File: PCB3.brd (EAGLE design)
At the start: 94.7 x 52.2 mm, 138 parts, among them U1 PIC32MX570F512L, Y1 16MHz

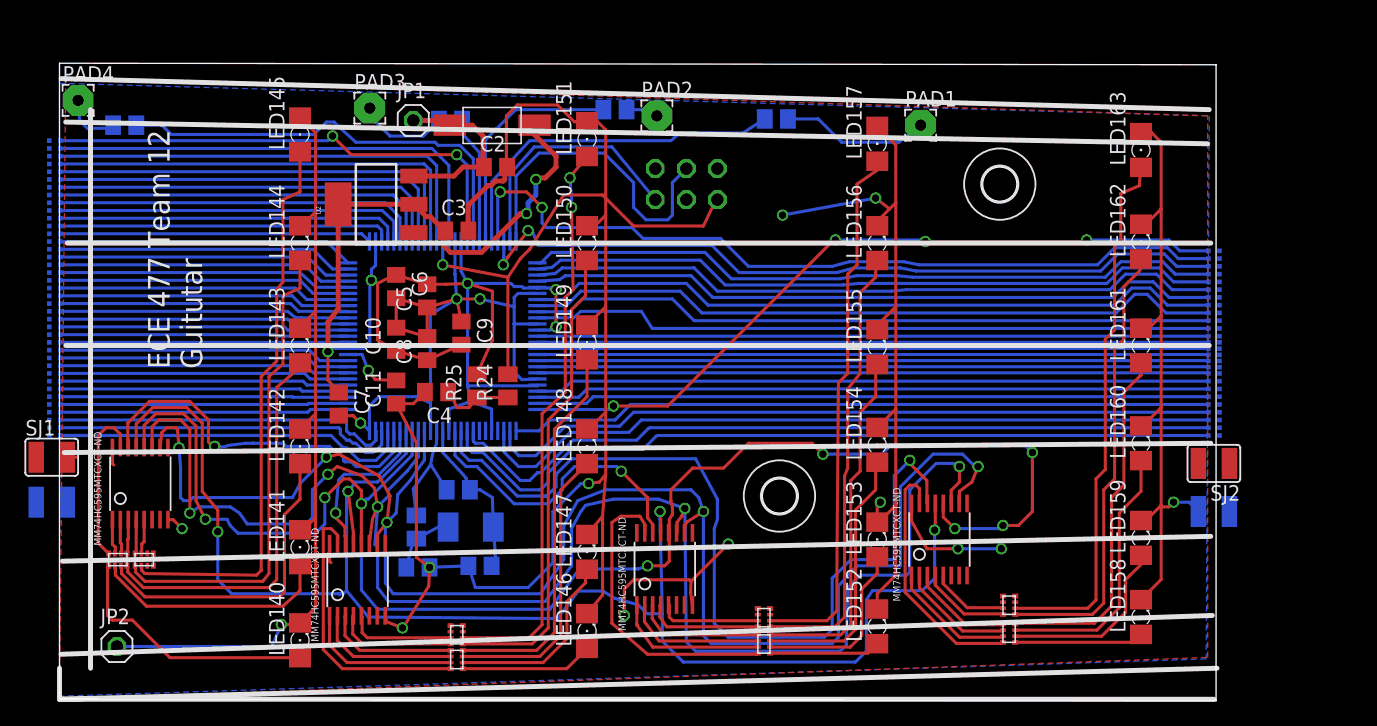
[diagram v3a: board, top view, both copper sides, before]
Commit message: Finished PCB3 checks and added traces for shift registers
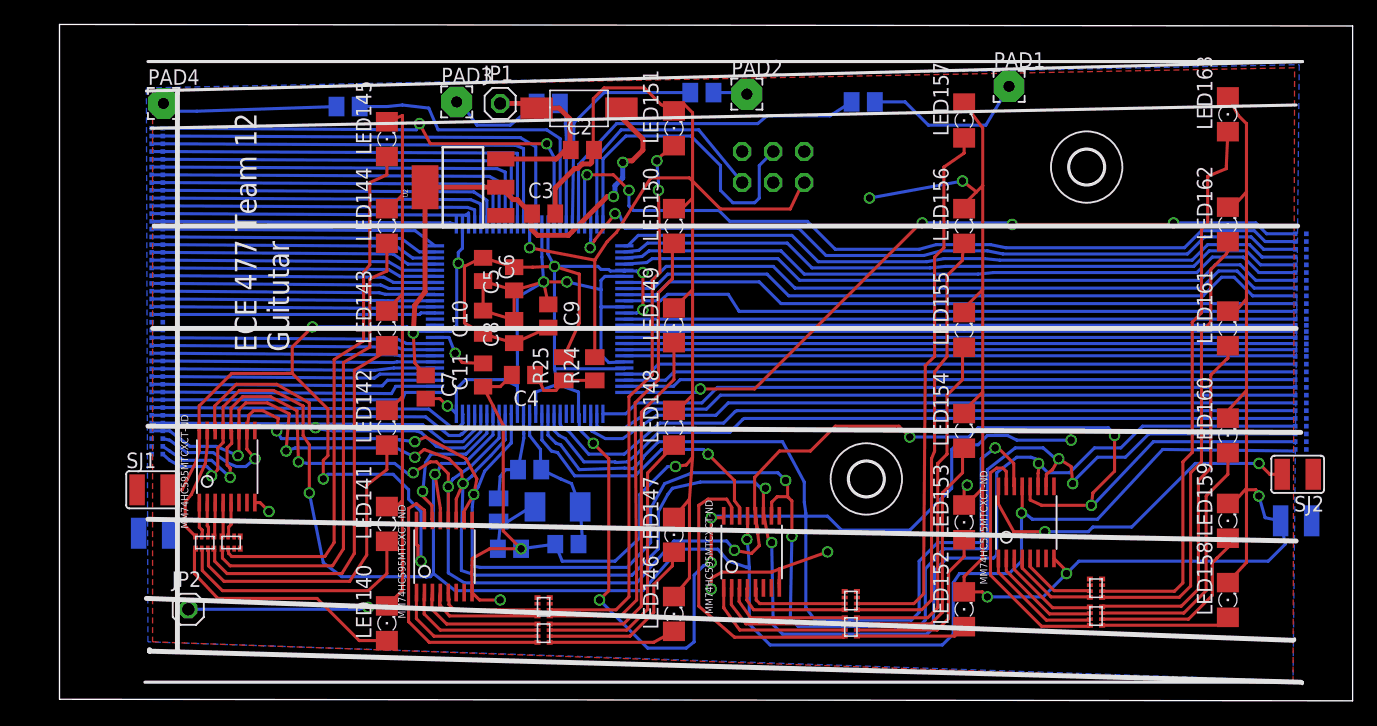
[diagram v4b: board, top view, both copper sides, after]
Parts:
- added RXD, U$2, U$79, U$80, U$81, U$82, U$83, U$84: JUMPER, ECE477_Guitutar:JUMPER
- moved R10 18.4 mm to (23.6, 48.5)
- moved SJ3 8.76 mm to (7.75, 13.6)
- moved SJ1 8.68 mm to (7.62, 17.1)
- moved U$43 8.44 mm to (8.00, 46.7)
- moved U$1 8.39 mm to (8.00, 44.8)
- moved U$10 8.39 mm to (8.00, 39.8)
- moved U$11 8.39 mm to (8.00, 39.1)
- moved U$12 8.39 mm to (8.00, 38.5)
- moved U$13 8.39 mm to (8.00, 37.8)
- moved U$14 8.39 mm to (8.00, 36.6)
- moved U$15 8.39 mm to (8.00, 37.2)
- moved U$16 8.39 mm to (8.00, 35.9)
- moved U$17 8.39 mm to (8.00, 35.3)
- moved U$18 8.39 mm to (8.00, 34.0)
- moved U$19 8.39 mm to (8.00, 34.7)
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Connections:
- net AMP: now also U$70.P$2
- net EAN: now also U$35.P$2
- net FRET1: now also U$18.P$2
- net FRET10: now also U$69.P$2
- net FRET11: now also U$48.P$2
- net FRET12: now also U$47.P$2
- net FRET13: now also U$52.P$2
- net FRET14: now also U$51.P$2
- net FRET15: now also U$56.P$2
- net FRET16: now also U$50.P$2
- net FRET17: now also U$55.P$2
- net FRET18: now also U$60.P$2
- net FRET19: now also U$59.P$2
- net FRET2: now also U$20.P$2
- net FRET20: now also U$58.P$2
- net FRET21: now also U$54.P$2
- net FRET22: now also U$64.P$2
- net FRET3: now also U$21.P$2
- net FRET4: now also U$22.P$2
- net FRET5: now also U$43.P$1, U$43.P$2
- net G: now also U$80.P$2, U$84.P$2
- net LED_SER1: now also U$12.P$2
- net LED_SER12: now also U$46.P$2
- net LED_SER13: now also U$53.P$2
- net LED_SER14: now also U$57.P$2
- net LED_SER15: now also U$49.P$2
- net LED_SER16: now also U$45.P$2
- net LED_SER17: now also U$63.P$2
- net LED_SER18: now also U$62.P$2
- net LED_SER19: now also U$61.P$2
- net LED_SER2: now also U$13.P$2
- net LED_SER20: now also U$68.P$2
- net LED_SER21: now also U$67.P$2
- net LED_SER22: now also U$66.P$2
- net LED_SER23: now also U$65.P$2
- net LED_SER3: now also U$15.P$2
- net LED_SER4: now also U$14.P$2
- net LED_SER5: now also U$38.P$2
- net LED_SER6: now also U$39.P$2
- net LED_SER7: now also U$40.P$2
- net P0_0: now also U$32.P$2
- net P0_4: now also U$10.P$2
- net P0_5: now also U$31.P$2
- net P1_2: now also U$37.P$2
- net P1_3: now also U$41.P$2
- net P1_5: now also U$11.P$2
- net P1_7: now also U$30.P$2
- net P2_0: now also U$33.P$2
- net P2_4: now also U$34.P$2
- net P3_1: now also U$1.P$2
- net P3_2: now also U$4.P$2
- net P3_3: now also U$3.P$2
- net P3_4: now also U$6.P$2
- net P3_6: now also U$5.P$2
- net P3_7: now also U$7.P$2
- net RCK: now also U$79.P$2, U$83.P$2
- net RST_N: now also U$36.P$2
- net RXD: now also RXD.P$1, RXD.P$2
- net SCK: now also U$42.P$1, U$42.P$2, U$81.P$1, U$81.P$2
- net SCLR: now also U$2.P$2, U$82.P$2
- net STRING1: now also U$16.P$2
- net STRING2: now also U$17.P$2
- net STRING3: now also U$19.P$2
- net STRING4: now also U$23.P$2
- net STRING5: now also U$24.P$2
- net STRING6: now also U$25.P$2
- net SW_BTN: now also U$9.P$2
- net TXD: now also U$44.P$1, U$44.P$2
- net WAKEUP: now also U$8.P$2
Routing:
- net VDD: track 138.8 -> 284.3 mm, vias 9 -> 17
- net GND: track 310.3 -> 343.7 mm, vias 11 -> 13
- net G: track 130.1 -> 159.2 mm, vias 4 -> 5
- net SCLR: track 132.0 -> 158.2 mm, vias 5 -> 8
- net STRING5: track 23.7 -> 0.00 mm
- net LED_SER7: track 51.8 -> 28.6 mm
- net RCK: track 130.9 -> 153.3 mm
- net STRING6: track 23.6 -> 1.35 mm
- net SCK: track 134.4 -> 154.1 mm, vias 5 -> 7
- net FRET6: track 36.3 -> 24.8 mm
- net N$7: track 4.76 -> 14.7 mm
- net N$31: track 13.4 -> 9.46 mm
- net N$47: track 46.3 -> 43.8 mm
- net OSC2: track 9.91 -> 8.14 mm
- net LED_SER8: track 71.3 -> 69.6 mm
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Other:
- board size 94.7 x 52.2 mm -> 105.8 x 55.4 mm

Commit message: Moved traces around. Added another hole for AMP input
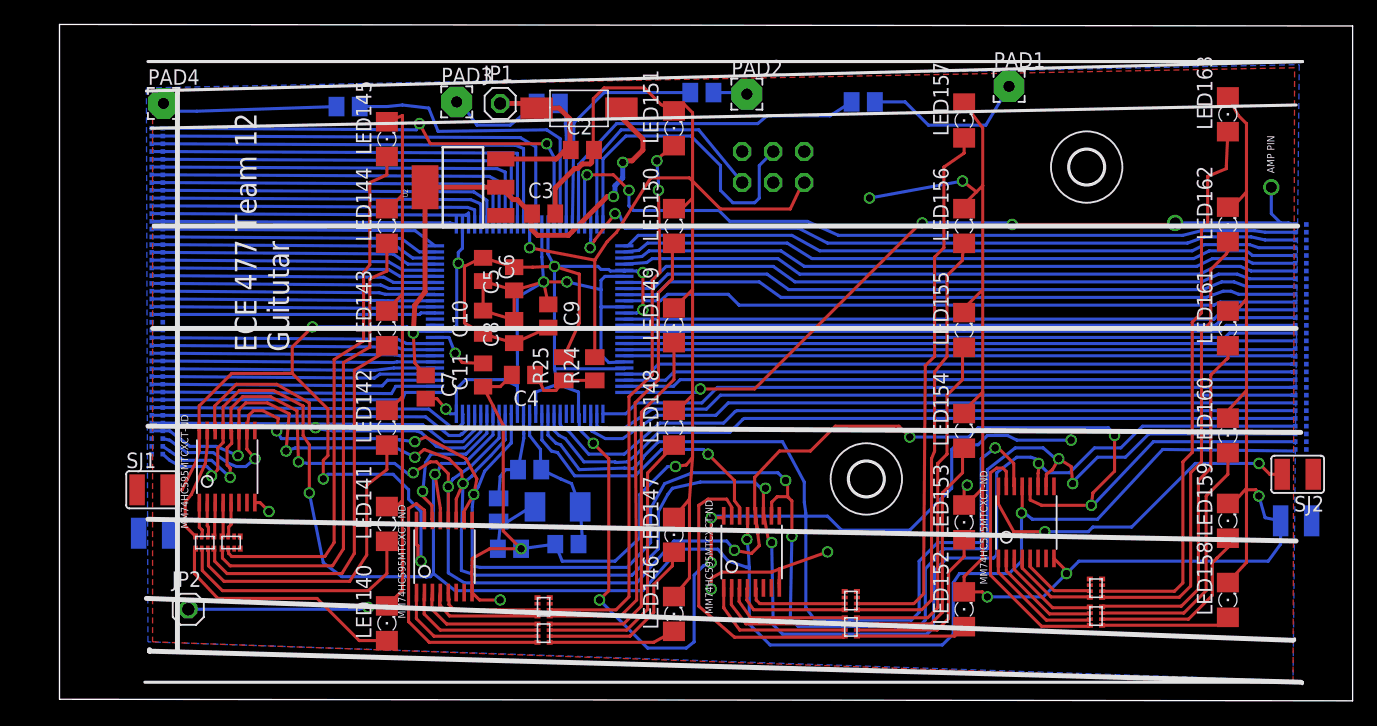
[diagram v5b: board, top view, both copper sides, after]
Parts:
- moved U$47 0.76 mm to (101.6, 37.0)
- moved U$48 0.76 mm to (101.6, 37.6)
- moved U$50 0.76 mm to (101.6, 34.4)
- moved U$51 0.76 mm to (101.6, 35.7)
- moved U$52 0.76 mm to (101.6, 36.3)
- moved U$56 0.76 mm to (101.6, 35.1)
- moved U$58 0.76 mm to (101.6, 31.9)
- moved U$59 0.76 mm to (101.6, 32.5)
- moved U$60 0.76 mm to (101.6, 33.1)
- moved U$70 0.76 mm to (101.6, 38.9)
- moved U$55 0.76 mm to (101.6, 33.8)
- moved U$69 0.76 mm to (101.6, 38.2)
- moved U$54 0.64 mm to (101.6, 31.2)
- moved U$64 0.51 mm to (101.6, 30.6)
- moved U$63 0.38 mm to (101.6, 30.0)
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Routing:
- net AMP: track 61.1 -> 64.0 mm, vias 4 -> 5
- net FRET10: track 66.3 -> 64.7 mm
- net FRET11: track 63.7 -> 62.2 mm
- net FRET17: track 57.4 -> 56.0 mm
- net FRET12: track 57.1 -> 55.8 mm
- net FRET16: track 57.3 -> 56.1 mm
- net FRET14: track 56.9 -> 55.7 mm
- net FRET13: track 56.9 -> 55.8 mm
- net FRET15: track 56.8 -> 55.7 mm
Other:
- board text added: "AMP PIN"

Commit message: Moved traces around. DRC check done
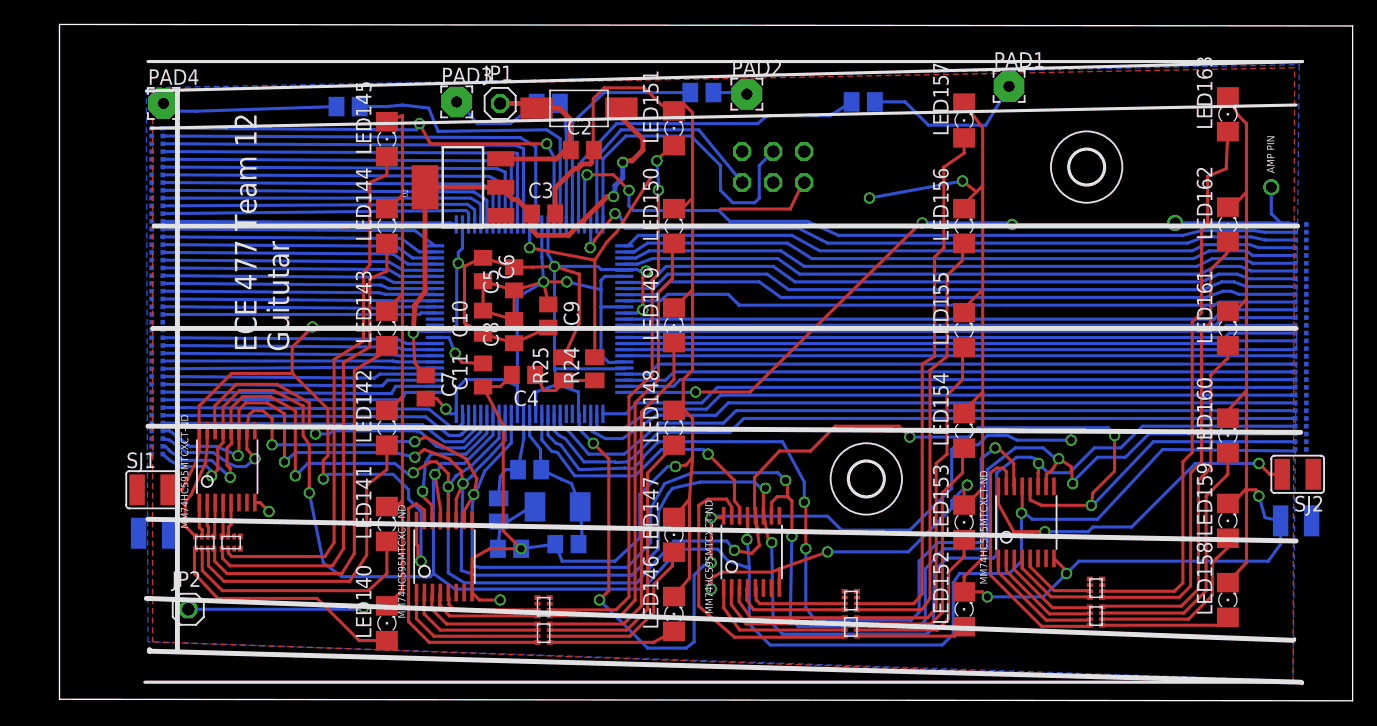
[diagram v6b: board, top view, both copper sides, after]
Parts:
- turned U$1 to 180 degrees
- turned U$10 to 180 degrees
- turned U$11 to 180 degrees
- turned U$12 to 180 degrees
- turned U$13 to 180 degrees
- turned U$14 to 180 degrees
- turned U$15 to 180 degrees
- turned U$16 to 180 degrees
- turned U$17 to 180 degrees
- turned U$18 to 180 degrees
- turned U$19 to 180 degrees
- turned U$20 to 180 degrees
- turned U$21 to 180 degrees
- turned U$22 to 180 degrees
- turned U$23 to 180 degrees
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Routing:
- net GND: track 343.4 -> 357.3 mm
- net N$13: track 38.8 -> 32.1 mm
- net RCK: track 153.3 -> 155.1 mm
- net P2_4: track 23.2 -> 22.3 mm
- net TXD: track 36.7 -> 35.8 mm
- net STRING1: track 23.4 -> 22.5 mm
- net RXD: track 38.0 -> 37.1 mm
- net RST_N: track 23.4 -> 22.5 mm
- net P3_7: track 29.6 -> 28.7 mm
- net P3_6: track 30.8 -> 29.9 mm
- net P3_4: track 32.1 -> 31.1 mm
- net P3_3: track 33.3 -> 32.4 mm
- net P3_2: track 34.5 -> 33.6 mm
- net P3_1: track 35.8 -> 34.8 mm
- net P1_7: track 23.3 -> 22.4 mm
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
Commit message: Finished PCB4. Finished gerbers for PCB1, 2, 3, and 4
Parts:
- moved LED158 2.92 mm to (95.8, 5.21)
- moved LED152 1.52 mm to (74.0, 5.84)
- moved LED159 1.40 mm to (95.6, 13.2)
- moved LED153 0.89 mm to (74.0, 13.6)
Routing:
- net GND: track 357.3 -> 364.4 mm
- net N$13: track 32.1 -> 38.8 mm, vias 1 -> 3
- net N$43: track 14.9 -> 14.0 mm
